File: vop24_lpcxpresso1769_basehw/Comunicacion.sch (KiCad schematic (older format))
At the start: 4 parts

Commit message: Esq Comunicacion: USB, BLE y UART resueltos. Falta ver control de alimentación de BLE en caso que no se pueda apagar
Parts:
- removed J?: USB_A, symbol Connector:USB_A
- added C?: 10uF, symbol Device:C
- added J?: USB_B_Micro, symbol Connector:USB_B_Micro
- added J?: Conn_01x05_Male, symbol Connector:Conn_01x05_Male
- added U?: TPD4S014, symbol tpd4s014:TPD4S014
- C?: value C -> 10n/500V
- R?: value R -> 1M
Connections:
- net labels added: BLE_EN, BLE_GND, BLE_RXD, BLE_STATE, BLE_TXD, BLE_VCC, TPD_~ACK, TPD_~EN, USB_D+, USB_D-, USB_ID, UU_5V, UU_GND, UU_RXD, UU_TXD, UU_VCC, VUSB_OUT
- wire segments 29 -> 40
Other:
- note added: "BLE HM10"
- note added: "UART USB Debug"
- note added: "USB"
- note removed: "hacer simbolo y footprint del tpd4s014\n"
- moved on the sheet: C?, J?, R?

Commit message: Primera versión esquematico sin revisar
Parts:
- added C31, C33: 0.1uF, symbol Device:C
- added C32, C36: 22uF/25V, symbol Device:C
- added C34: 0.22uF, symbol Device:C
- added C35: 2.2uF CER, symbol Device:C
- added D3, D4: MBRS130LT3, symbol Device:D_Schottky
- added J12: Screw_Terminal_01x02, symbol Connector:Screw_Terminal_01x02
- added L2: L_Core_Ferrite_Coupled, symbol Device:L_Core_Ferrite_Coupled
- added R30, R35, R36: 1M, symbol Device:R
- added R31: 1k, symbol Device:R
- added R32: 0, symbol Device:R
- added R33: 24, symbol Device:R
- added R34: 0.2, symbol Device:R
- added U12: LTC4411, symbol cargaBateriaUSB:LTC4411
- added U13: LT1512, symbol cargaBateriaUSB:LT1512
- gave numbers to parts that had none: 7
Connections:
- net labels added: GND_SW, LTC4411_STAT, S-S, USB_GND, VBAT+, VBAT-, VCC_SW, VOUTR, coilA
- wire segments 40 -> 124
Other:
- note added: "CARGA DE BATERIA\n"
- note added: "Divisor resistivo\npara calcular corriente\nde carga de batería"
- note added: "PUERTO USB\n"
- note added: "SWITCH ENTRE\nBATERIA Y VUSB\n"
- note added: "VER COMO HACER CON LOS PINES CORTOCIRCUITADOS INTERNAMENTE EN EL TPD\n"
- note added: "de la hoja de datos: \nTOKIN CERAMIC \n1E225ZY5U-C203-F\n"
- moved on the sheet: C29, C30, J10, J11, J9, R29, U11

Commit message: Algunas correcciones sobre el esquemático. Falta terminar de revisar algunos conflictos del DRC
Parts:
- renumbered C29 to C301, C30 to C302, C31 to C303, C32 to C304, C33 to C305, C34 to C306, C35 to C307, C36 to C308, D3 to D301, D4 to D302, J9 to J301, J10 to J302, J11 to J303, J12 to J304, L2 to L301, R29 to R301, R30 to R302, R31 to R303, R32 to R304, R33 to R305, R34 to R306, R35 to R307, R36 to R308, U11 to U301, U12 to U302, U13 to U303
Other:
- moved on the sheet: R304
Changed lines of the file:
@@
 	1000 4200 1000 4350
 $Comp
-L Device:R R29
+L Device:R R301
 U 1 1 5B9F0B88
 P 1000 4550
-F 0 "R29" H 1070 4596 50  0000 L CNN
+F 0 "R301" H 1070 4596 50  0000 L CNN
 F 1 "1M" H 1070 4505 50  0000 L CNN
 F 2 "" V 930 4550 50  0001 C CNN
@@
 $EndComp
 $Comp
-L Device:C C29
+L Device:C C301
 U 1 1 5B9F0BDD
 P 1300 4550
-F 0 "C29" H 1415 4596 50  0000 L CNN
+F 0 "C301" H 1415 4596 50  0000 L CNN
 F 1 "10n/500V" H 1415 4505 50  0000 L CNN
 F 2 "" H 1338 4400 50  0001 C CNN
@@
 	1550 4250 1550 4750
 $Comp
-L Connector:Conn_01x06_Male J10
+L Connector:Conn_01x06_Male J302
 U 1 1 5BA01F94
 P 3300 1550
-F 0 "J10" H 3406 1928 50  0000 C CNN
+F 0 "J302" H 3406 1928 50  0000 C CNN
 F 1 "Conn_01x06_Male" H 3406 1837 50  0000 C CNN
 F 2 "" H 3300 1550 50  0001 C CNN
@@
 	1400 3800 2400 3800
 $Comp
-L Connector:USB_B_Micro J9
+L Connector:USB_B_Micro J301
 U 1 1 5BAE3529
 P 1100 3800
-F 0 "J9" H 1155 4267 50  0000 C CNN
+F 0 "J301" H 1155 4267 50  0000 C CNN
 F 1 "USB_B_Micro" H 1155 4176 50  0000 C CNN
 F 2 "" H 1250 3750 50  0001 C CNN
@@
 $EndComp
 $Comp
-L tpd4s014:TPD4S014 U11
+L tpd4s014:TPD4S014 U301
 U 1 1 5BAE3ACE
 P 2400 3250
-F 0 "U11" H 2700 3600 50  0000 C CNN
+F 0 "U301" H 2700 3600 50  0000 C CNN
 F 1 "TPD4S014" H 2350 3600 50  0000 C CNN
 F 2 "" H 2250 3250 50  0001 C CNN
@@
 	1550 3050 1700 3050
 $Comp
-L power:GND #PWR025
+L power:GND #PWR0301
 U 1 1 5BAE503D
 P 1700 3500
-F 0 "#PWR025" H 1700 3250 50  0001 C CNN
+F 0 "#PWR0301" H 1700 3250 50  0001 C CNN
 F 1 "GND" H 1705 3327 50  0000 C CNN
 F 2 "" H 1700 3500 50  0001 C CNN
@@
 UU_VCC
 $Comp
-L Connector:Conn_01x05_Male J11
+L Connector:Conn_01x05_Male J303
 U 1 1 5BAF1C86
 P 5700 1550
-F 0 "J11" H 5806 1928 50  0000 C CNN
+F 0 "J303" H 5806 1928 50  0000 C CNN
 F 1 "Conn_01x05_Male" H 5806 1837 50  0000 C CNN
 F 2 "" H 5700 1550 50  0001 C CNN
@@
 VER COMO HACER CON LOS PINES CORTOCIRCUITADOS INTERNAMENTE EN EL TPD\n
 $Comp
-L Device:R R30
+L Device:R R302
 U 1 1 5BB133EA
 P 3100 2850
-F 0 "R30" H 3170 2896 50  0000 L CNN
+F 0 "R302" H 3170 2896 50  0000 L CNN
 F 1 "1M" H 3170 2805 50  0000 L CNN
 F 2 "" V 3030 2850 50  0001 C CNN
@@
 	3100 3350 3600 3350
 $Comp
-L cargaBateriaUSB:LT1512 U13
+L cargaBateriaUSB:LT1512 U303
 U 1 1 5BC34D77
 P 6300 3550
-F 0 "U13" H 6650 3950 50  0000 C CNN
+F 0 "U303" H 6650 3950 50  0000 C CNN
 F 1 "LT1512" H 6500 3800 50  0000 C CNN
 F 2 "" H 6300 3550 50  0001 C CNN
@@
 $EndComp
 $Comp
-L Device:C C32
+L Device:C C304
 U 1 1 5BC34DFA
 P 5200 4000
-F 0 "C32" H 5315 4046 50  0000 L CNN
+F 0 "C304" H 5315 4046 50  0000 L CNN
 F 1 "22uF/25V" H 5315 3955 50  0000 L CNN
 F 2 "" H 5238 3850 50  0001 C CNN
@@
 $EndComp
 $Comp
-L Device:C C33
+L Device:C C305
 U 1 1 5BC34E82
 P 6350 4150
-F 0 "C33" H 6465 4196 50  0000 L CNN
+F 0 "C305" H 6465 4196 50  0000 L CNN
 F 1 "0.1uF" H 6465 4105 50  0000 L CNN
 F 2 "" H 6388 4000 50  0001 C CNN
@@
 $EndComp
 $Comp
-L Device:C C34
+L Device:C C306
 U 1 1 5BC34EDA
 P 6650 4550
-F 0 "C34" H 6765 4596 50  0000 L CNN
+F 0 "C306" H 6765 4596 50  0000 L CNN
 F 1 "0.22uF" H 6765 4505 50  0000 L CNN
 F 2 "" H 6688 4400 50  0001 C CNN
@@
 $EndComp
 $Comp
-L Device:C C35
+L Device:C C307
 U 1 1 5BC34F18
 P 7250 3450
-F 0 "C35" H 7365 3496 50  0000 L CNN
+F 0 "C307" H 7365 3496 50  0000 L CNN
 F 1 "2.2uF CER" H 7365 3405 50  0000 L CNN
 F 2 "" H 7288 3300 50  0001 C CNN
@@
 $EndComp
 $Comp
-L Device:C C36
+L Device:C C308
 U 1 1 5BC34FB2
 P 8300 4250
-F 0 "C36" H 8415 4296 50  0000 L CNN
+F 0 "C308" H 8415 4296 50  0000 L CNN
 F 1 "22uF/25V" H 8415 4205 50  0000 L CNN
 F 2 "" H 8338 4100 50  0001 C CNN
@@
 de la hoja de datos: \nTOKIN CERAMIC \n1E225ZY5U-C203-F\n
 $Comp
-L Device:R R31
+L Device:R R303
 U 1 1 5BC35392
 P 6350 4550
-F 0 "R31" H 6420 4596 50  0000 L CNN
+F 0 "R303" H 6420 4596 50  0000 L CNN
 F 1 "1k" H 6420 4505 50  0000 L CNN
 F 2 "" V 6280 4550 50  0001 C CNN
@@
 $EndComp
 $Comp
-L Device:R R34
+L Device:R R306
 U 1 1 5BC35474
 P 7450 4550
-F 0 "R34" H 7520 4596 50  0000 L CNN
+F 0 "R306" H 7520 4596 50  0000 L CNN
 F 1 "0.2" H 7520 4505 50  0000 L CNN
 F 2 "" V 7380 4550 50  0001 C CNN
@@
 $EndComp
 $Comp
-L Device:R R33
+L Device:R R305
 U 1 1 5BC35500
 P 7050 4300
-F 0 "R33" H 7120 4346 50  0000 L CNN
+F 0 "R305" H 7120 4346 50  0000 L CNN
 F 1 "24" H 7120 4255 50  0000 L CNN
 F 2 "" V 6980 4300 50  0001 C CNN
@@
 $EndComp
 $Comp
-L Device:R R35
+L Device:R R307
 U 1 1 5BC355AC
 P 8000 3750
-F 0 "R35" H 8070 3796 50  0000 L CNN
+F 0 "R307" H 8070 3796 50  0000 L CNN
 F 1 "1M" H 8070 3705 50  0000 L CNN
 F 2 "" V 7930 3750 50  0001 C CNN
@@
 $EndComp
 $Comp
-L Device:R R36
+L Device:R R308
 U 1 1 5BC3560A
 P 8000 4400
-F 0 "R36" H 8070 4446 50  0000 L CNN
+F 0 "R308" H 8070 4446 50  0000 L CNN
 F 1 "1M" H 8070 4355 50  0000 L CNN
 F 2 "" V 7930 4400 50  0001 C CNN
@@
 Divisor resistivo\npara calcular corriente\nde carga de batería
 $Comp
-L Device:L_Core_Ferrite_Coupled L2
+L Device:L_Core_Ferrite_Coupled L301
 U 1 1 5BC35BED
 P 6600 2750
-F 0 "L2" H 6600 3028 50  0000 C CNN
+F 0 "L301" H 6600 3028 50  0000 C CNN
 F 1 "L_Core_Ferrite_Coupled" H 6600 2937 50  0000 C CNN
 F 2 "" H 6600 2750 50  0001 C CNN
@@
 coilA
 $Comp
-L Device:D_Schottky D4
+L Device:D_Schottky D302
 U 1 1 5BC4D3CD
 P 7750 3450
-F 0 "D4" H 7750 3234 50  0000 C CNN
+F 0 "D302" H 7750 3234 50  0000 C CNN
 F 1 "MBRS130LT3" H 7600 3350 50  0000 C CNN
 F 2 "" H 7750 3450 50  0001 C CNN
@@
 Wire Wire Line
 	5600 3500 5450 3500
-Text GLabel 5450 3500 0    50   Input ~ 0
-S-S
 Wire Wire Line
 	5200 2850 4800 2850
@@
 	5200 4800 4800 4800
 Connection ~ 5200 4800
-Text Label 4800 4800 0    50   ~ 0
-USB_GND
 Text Label 4850 2850 0    50   ~ 0
 VUSB_OUT
 $Comp
-L cargaBateriaUSB:LTC4411 U12
+L cargaBateriaUSB:LTC4411 U302
 U 1 1 5BCCEE8C
 P 3250 6600
-F 0 "U12" H 3450 6950 50  0000 C CNN
+F 0 "U302" H 3450 6950 50  0000 C CNN
 F 1 "LTC4411" H 3250 6800 50  0000 C CNN
 F 2 "" H 3200 6550 50  0001 C CNN
@@
 $EndComp
 $Comp
-L Device:D_Schottky D3
+L Device:D_Schottky D301
 U 1 1 5BCCF0A2
 P 3250 6100
-F 0 "D3" H 3250 5884 50  0000 C CNN
+F 0 "D301" H 3250 5884 50  0000 C CNN
 F 1 "MBRS130LT3" H 3100 6000 50  0000 C CNN
 F 2 "" H 3250 6100 50  0001 C CNN
@@
 Connection ~ 3750 6100
 $Comp
-L Device:C C31
+L Device:C C303
 U 1 1 5BCE020F
 P 3950 6400
-F 0 "C31" H 4065 6446 50  0000 L CNN
+F 0 "C303" H 4065 6446 50  0000 L CNN
 F 1 "0.1uF" H 4065 6355 50  0000 L CNN
 F 2 "" H 3988 6250 50  0001 C CNN
@@
 Wire Wire Line
 	2750 6750 2750 7000
-Text GLabel 3700 6750 2    50   Input ~ 0
-LTC4411_STAT
 Text Label 2600 6550 0    50   ~ 0
 VBAT+
@@
 VUSB_OUT
 $Comp
-L Device:R R32
+L Device:R R304
 U 1 1 5BCF71FC
-P 6900 5850
-F 0 "R32" H 6970 5896 50  0000 L CNN
-F 1 "0" H 6970 5805 50  0000 L CNN
-F 2 "" V 6830 5850 50  0001 C CNN
-F 3 "~" H 6900 5850 50  0001 C CNN
-	1    6900 5850
+P 5500 5100
+F 0 "R304" V 5350 4950 50  0000 L CNN
+F 1 "0" V 5500 5100 50  0000 L CNN
+F 2 "" V 5430 5100 50  0001 C CNN
+F 3 "~" H 5500 5100 50  0001 C CNN
+	1    5500 5100
 	0    1    1    0
 $EndComp
 Wire Wire Line
-	6750 5850 6250 5850
-Text Label 6350 5850 0    50   ~ 0
+	5350 5100 4850 5100
+Text Label 4950 5100 0    50   ~ 0
 VBAT-
 Wire Wire Line
-	7050 5850 7500 5850
-Text Label 7150 5850 0    50   ~ 0
+	5650 5100 6100 5100
+Text Label 5750 5100 0    50   ~ 0
 USB_GND
 Wire Wire Line
@@
 	1300 4750 1550 4750
 $Comp
-L Device:C C30
+L Device:C C302
 U 1 1 5BAE49F4
 P 1700 3300
-F 0 "C30" H 1750 3500 50  0000 L CNN
+F 0 "C302" H 1750 3500 50  0000 L CNN
 F 1 "10uF" H 1750 3400 50  0000 L CNN
 F 2 "" H 1738 3150 50  0001 C CNN
@@
 	1700 3050 1900 3050
 Wire Notes Line
-	9150 2350 9150 5000
-Wire Notes Line
-	9150 5000 4650 5000
-Wire Notes Line
-	4650 5000 4650 2350
+	9150 2350 9150 5350
+Wire Notes Line
+	9150 5350 4650 5350
+Wire Notes Line
+	4650 5350 4650 2350
 Wire Notes Line
 	4650 2350 9150 2350
@@
 GND_SW
 $Comp
-L Connector:Screw_Terminal_01x02 J12
+L Connector:Screw_Terminal_01x02 J304
 U 1 1 5BDFE4B3
 P 8950 4200
-F 0 "J12" H 9030 4192 50  0000 L CNN
+F 0 "J304" H 9030 4192 50  0000 L CNN
 F 1 "Screw_Terminal_01x02" H 9030 4101 50  0000 L CNN
 F 2 "" H 8950 4200 50  0001 C CNN
@@
 Wire Wire Line
 	2950 3050 3600 3050
+Text HLabel 3700 6750 2    50   Input ~ 0
+LTC4411_STAT
+Text HLabel 5450 3500 0    50   Input ~ 0
+S-S
 $EndSCHEMATC

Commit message: Correcciones de esquemático:    - resueltos todos los conflictos de DRC    - cambio de circutio de medicion de temp    - ordenados todas las etiquetas y valores
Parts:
- renumbered R304 to R303, R303 to R304
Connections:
- net labels added: DGND, LT1512_S-S
- net labels removed: GND, S-S
- wire segments 124 -> 125
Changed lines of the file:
@@
 Wire Wire Line
 	1550 3050 1700 3050
-$Comp
-L power:GND #PWR0301
-U 1 1 5BAE503D
-P 1700 3500
-F 0 "#PWR0301" H 1700 3250 50  0001 C CNN
-F 1 "GND" H 1705 3327 50  0000 C CNN
-F 2 "" H 1700 3500 50  0001 C CNN
-F 3 "" H 1700 3500 50  0001 C CNN
-	1    1700 3500
-	1    0    0    -1
-$EndComp
-Wire Wire Line
-	1700 3500 1700 3450
 Wire Wire Line
 	2900 3050 2950 3050
@@
 U 1 1 5BC34F18
 P 7250 3450
-F 0 "C307" H 7365 3496 50  0000 L CNN
-F 1 "2.2uF CER" H 7365 3405 50  0000 L CNN
+F 0 "C307" V 7100 3300 50  0000 L CNN
+F 1 "2.2uF CER" V 7365 3405 50  0000 L CNN
 F 2 "" H 7288 3300 50  0001 C CNN
 F 3 "~" H 7250 3450 50  0001 C CNN
@@
 de la hoja de datos: \nTOKIN CERAMIC \n1E225ZY5U-C203-F\n
 $Comp
-L Device:R R303
+L Device:R R304
 U 1 1 5BC35392
 P 6350 4550
-F 0 "R303" H 6420 4596 50  0000 L CNN
+F 0 "R304" H 6420 4596 50  0000 L CNN
 F 1 "1k" H 6420 4505 50  0000 L CNN
 F 2 "" V 6280 4550 50  0001 C CNN
@@
 U 1 1 5BC35474
 P 7450 4550
-F 0 "R306" H 7520 4596 50  0000 L CNN
-F 1 "0.2" H 7520 4505 50  0000 L CNN
+F 0 "R306" H 7500 4500 50  0000 L CNN
+F 1 "0.2" H 7550 4600 50  0000 L CNN
 F 2 "" V 7380 4550 50  0001 C CNN
 F 3 "~" H 7450 4550 50  0001 C CNN
@@
 U 1 1 5BC35500
 P 7050 4300
-F 0 "R305" H 7120 4346 50  0000 L CNN
-F 1 "24" H 7120 4255 50  0000 L CNN
+F 0 "R305" V 6900 4150 50  0000 L CNN
+F 1 "24" V 6900 4400 50  0000 L CNN
 F 2 "" V 6980 4300 50  0001 C CNN
 F 3 "~" H 7050 4300 50  0001 C CNN
@@
 U 1 1 5BC355AC
 P 8000 3750
-F 0 "R307" H 8070 3796 50  0000 L CNN
-F 1 "1M" H 8070 3705 50  0000 L CNN
+F 0 "R307" H 8100 3700 50  0000 L CNN
+F 1 "1M" H 8100 3800 50  0000 L CNN
 F 2 "" V 7930 3750 50  0001 C CNN
 F 3 "~" H 8000 3750 50  0001 C CNN
@@
 U 1 1 5BC3560A
 P 8000 4400
-F 0 "R308" H 8070 4446 50  0000 L CNN
-F 1 "1M" H 8070 4355 50  0000 L CNN
+F 0 "R308" H 8100 4350 50  0000 L CNN
+F 1 "1M" H 8100 4450 50  0000 L CNN
 F 2 "" V 7930 4400 50  0001 C CNN
 F 3 "~" H 8000 4400 50  0001 C CNN
@@
 VUSB_OUT
 $Comp
-L Device:R R304
+L Device:R R303
 U 1 1 5BCF71FC
 P 5500 5100
-F 0 "R304" V 5350 4950 50  0000 L CNN
+F 0 "R303" V 5350 4950 50  0000 L CNN
 F 1 "0" V 5500 5100 50  0000 L CNN
 F 2 "" V 5430 5100 50  0001 C CNN
@@
 LTC4411_STAT
 Text HLabel 5450 3500 0    50   Input ~ 0
-S-S
+LT1512_S-S
+Wire Wire Line
+	1700 3700 1450 3700
+Wire Wire Line
+	1700 3450 1700 3700
+Text Label 1500 3700 0    50   ~ 0
+DGND
 $EndSCHEMATC

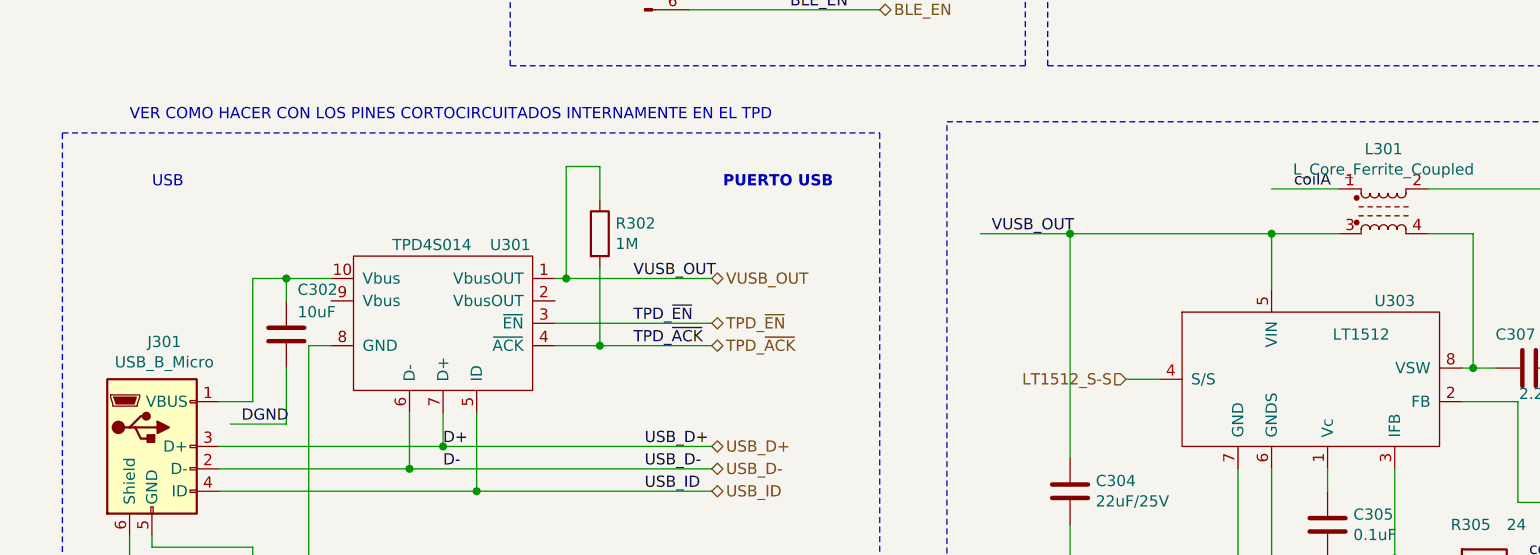
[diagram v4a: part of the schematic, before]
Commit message: Se agregaron la mayoría de los footprints de los ICs
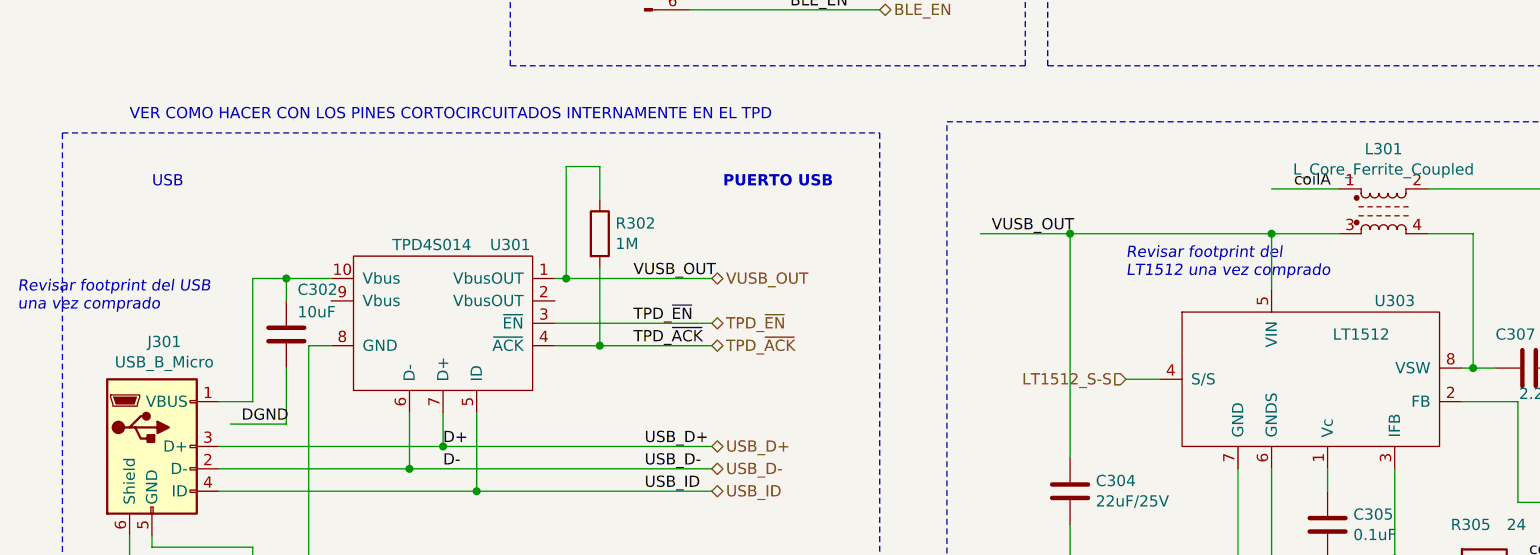
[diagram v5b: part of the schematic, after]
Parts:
- D301: footprint (none) -> Diode_SMD:D_SMB-SMC_Universal_Handsoldering
- J301: footprint (none) -> Connector_USB:USB_Mini-B_Lumberg_2486_01_Horizontal
- U301: footprint (none) -> Package_SON:Texas_S-PWSON-N10
- U302: footprint (none) -> Package_TO_SOT_SMD:TSOT-23-5_HandSoldering
- U303: footprint (none) -> Package_SO:SO-8_5.3x6.2mm_P1.27mm
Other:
- note added: "Revisar footprint del USB \nuna vez comprado"
- note added: "Revisar footprint del \nLT1512 una vez comprado"
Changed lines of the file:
@@
 F 0 "J301" H 1155 4267 50  0000 C CNN
 F 1 "USB_B_Micro" H 1155 4176 50  0000 C CNN
-F 2 "" H 1250 3750 50  0001 C CNN
+F 2 "Connector_USB:USB_Mini-B_Lumberg_2486_01_Horizontal" H 1250 3750 50  0001 C CNN
 F 3 "~" H 1250 3750 50  0001 C CNN
 	1    1100 3800
@@
 F 0 "U301" H 2700 3600 50  0000 C CNN
 F 1 "TPD4S014" H 2350 3600 50  0000 C CNN
-F 2 "" H 2250 3250 50  0001 C CNN
+F 2 "Package_SON:Texas_S-PWSON-N10" H 2250 3250 50  0001 C CNN
 F 3 "/home/froux/Dropbox/VOP24/docs y hojas de datos/otros/cosas modulo usb/tpd4s014.pdf" H 2250 3250 50  0001 C CNN
 	1    2400 3250
@@
 F 0 "U303" H 6650 3950 50  0000 C CNN
 F 1 "LT1512" H 6500 3800 50  0000 C CNN
-F 2 "" H 6300 3550 50  0001 C CNN
+F 2 "Package_SO:SO-8_5.3x6.2mm_P1.27mm" H 6300 3550 50  0001 C CNN
 F 3 "" H 6300 3550 50  0001 C CNN
 	1    6300 3550
@@
 F 0 "U302" H 3450 6950 50  0000 C CNN
 F 1 "LTC4411" H 3250 6800 50  0000 C CNN
-F 2 "" H 3200 6550 50  0001 C CNN
+F 2 "Package_TO_SOT_SMD:TSOT-23-5_HandSoldering" H 3200 6550 50  0001 C CNN
 F 3 "" H 3200 6550 50  0001 C CNN
 	1    3250 6600
@@
 F 0 "D301" H 3250 5884 50  0000 C CNN
 F 1 "MBRS130LT3" H 3100 6000 50  0000 C CNN
-F 2 "" H 3250 6100 50  0001 C CNN
+F 2 "Diode_SMD:D_SMB-SMC_Universal_Handsoldering" H 3250 6100 50  0001 C CNN
 F 3 "~" H 3250 6100 50  0001 C CNN
 	1    3250 6100
@@
 Text Label 1500 3700 0    50   ~ 0
 DGND
+Text Notes 500  3200 0    50   Italic 0
+Revisar footprint del USB \nuna vez comprado
+Text Notes 5450 3050 0    50   Italic 0
+Revisar footprint del \nLT1512 una vez comprado
 $EndSCHEMATC
